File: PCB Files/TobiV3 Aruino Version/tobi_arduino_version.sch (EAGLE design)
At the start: 56 parts, among them M1 M1_M2, M2 M1_M2, M3 DF11-4PIN, M4 DF11-4PIN, M5 DF11-4PIN, M6 DF11-4PIN

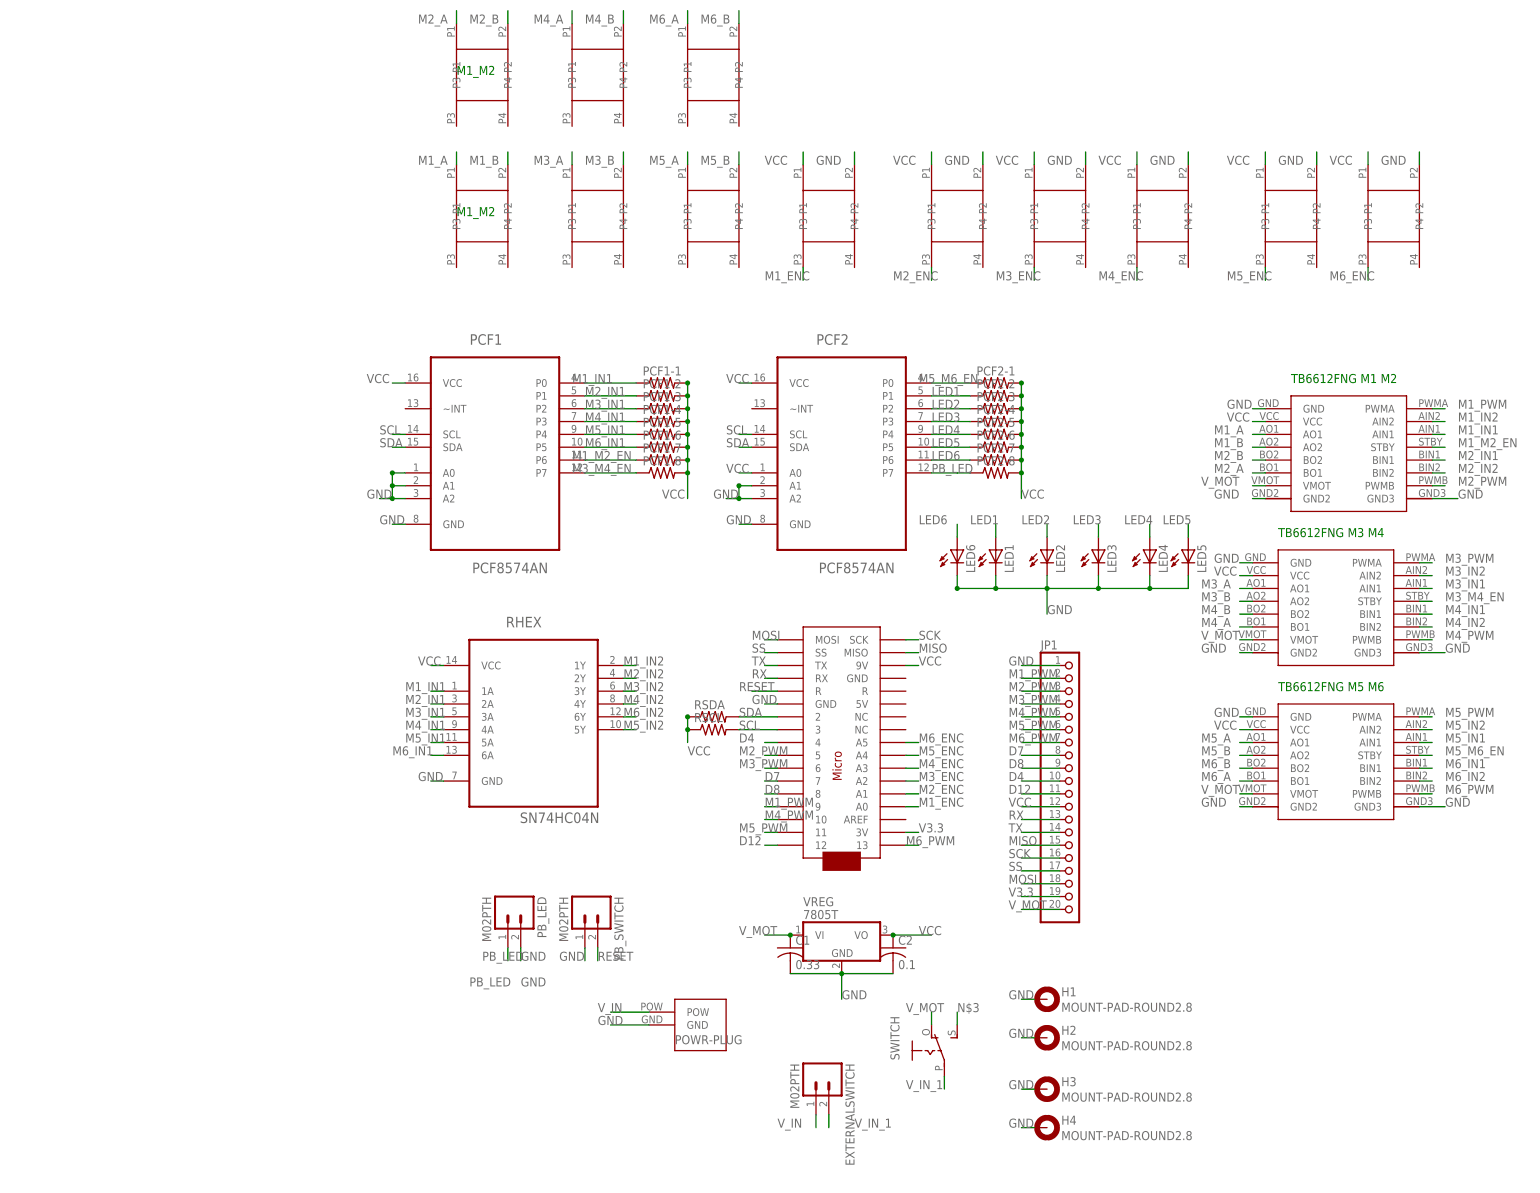
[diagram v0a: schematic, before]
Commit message: removed hex encoder, moved to 0-based
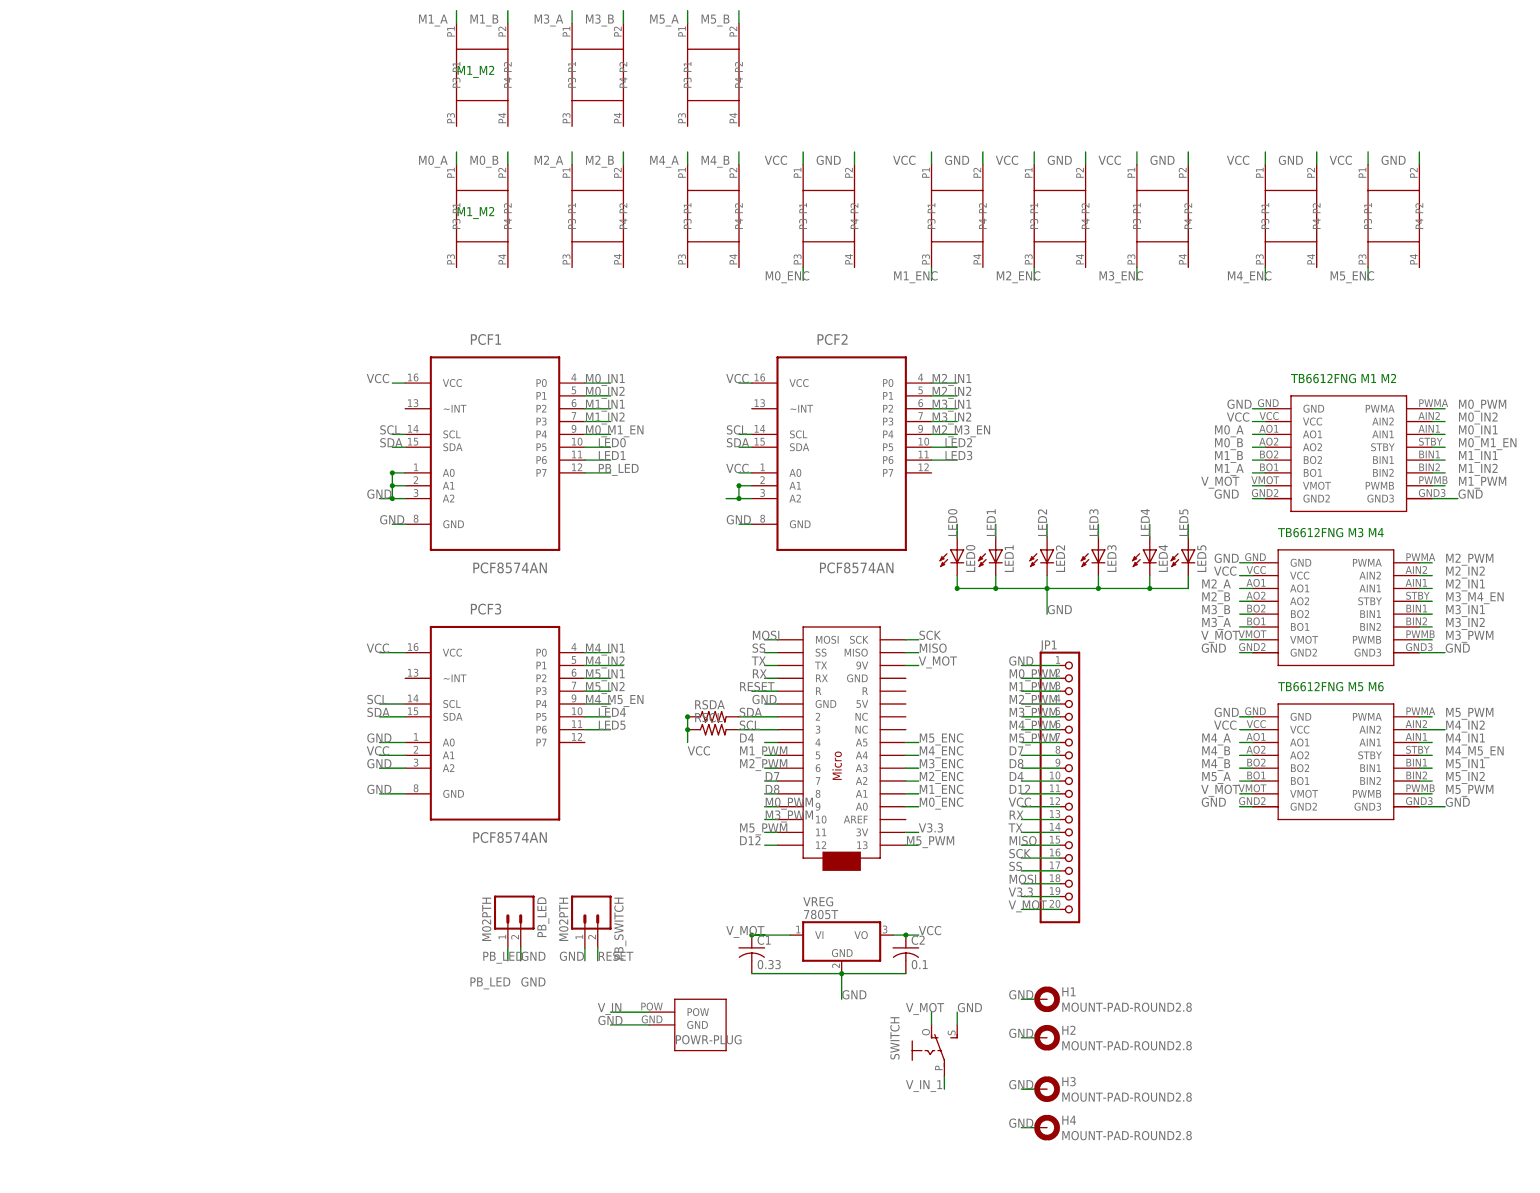
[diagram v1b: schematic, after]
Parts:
- removed EXTERNALSWITCH: M02PTH, SparkFun-Connectors:M02PTH
- removed PCF1-1, PCF1-2, PCF1-3, PCF1-4, PCF1-5, PCF1-6, PCF1-7, PCF1-8, PCF2-1, PCF2-2, PCF2-3, PCF2-4, PCF2-5, PCF2-6, PCF2-7, PCF2-8: (no value), rcl:R-US_0207/7
- removed RHEX: SN74HC04N, Texas Instruments_By_element14_Batch_1:SN74HC04N
- added PCF3: PCF8574AN, Texas Instruments_By_element14_Batch_1:PCF8574AN
- renumbered LED6 to LED0
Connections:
- removed net LED6: LED0.A, PCF2-7.1, PCF2.P6
- removed net M1_M2_EN: DRIVER1.STBY, PCF1-7.1, PCF1.P6
- removed net M5_M6_EN: DRIVER3.STBY, PCF2-1.1, PCF2.P0
- removed net M6_A: DRIVER3.BO1, M6.P1
- removed net M6_B: DRIVER3.BO2, M6.P2
- removed net M6_ENC: ARDUINOMICRO.A5, ENC6.P3
- removed net M6_IN1: DRIVER3.BIN1, PCF1-6.1, PCF1.P5, RHEX.6A
- removed net M6_IN2: DRIVER3.BIN2, RHEX.6Y
- removed net M6_PWM: ARDUINOMICRO.13, DRIVER3.PWMB, JP1.7
- removed net N$3: SWITCH.S
- new net LED0: LED0.A, PCF1.P5
- new net M0_A: DRIVER1.AO1, M1.P1
- new net M0_B: DRIVER1.AO2, M1.P2
- new net M0_ENC: ARDUINOMICRO.A0, ENC1.P3
- new net M0_IN1: DRIVER1.AIN1, PCF1.P0
- new net M0_IN2: DRIVER1.AIN2, PCF1.P1
- new net M0_M1_EN: DRIVER1.STBY, PCF1.P4
- new net M0_PWM: ARDUINOMICRO.9, DRIVER1.PWMA, JP1.2
- new net M2_M3_EN: PCF2.P4
- new net M4_M5_EN: DRIVER3.STBY, PCF3.P4
- net GND: now also PCF3.A0, PCF3.A2, PCF3.GND, SWITCH.S; no longer RHEX.GND
- net LED1: now also PCF1.P6; no longer PCF2-2.1, PCF2.P1
- net LED2: now also PCF2.P5; no longer PCF2-3.1, PCF2.P2
- net LED3: now also PCF2.P6; no longer PCF2-4.1, PCF2.P3
- net LED4: now also PCF3.P5; no longer PCF2-5.1, PCF2.P4
- net LED5: now also PCF3.P6; no longer PCF2-6.1, PCF2.P5
- net M1_A: now also DRIVER1.BO1, M2.P1; no longer DRIVER1.AO1, M1.P1
- net M1_B: now also DRIVER1.BO2, M2.P2; no longer DRIVER1.AO2, M1.P2
- net M1_ENC: now also ARDUINOMICRO.A1, ENC2.P3; no longer ARDUINOMICRO.A0, ENC1.P3
- net M1_IN1: now also DRIVER1.BIN1, PCF1.P2; no longer DRIVER1.AIN1, PCF1-1.1, PCF1.P0, RHEX.1A
- net M1_IN2: now also DRIVER1.BIN2, PCF1.P3; no longer DRIVER1.AIN2, RHEX.1Y
- net M1_PWM: now also ARDUINOMICRO.5, DRIVER1.PWMB, JP1.3; no longer ARDUINOMICRO.9, DRIVER1.PWMA, JP1.2
- net M2_A: now also DRIVER2.AO1, M3.P1; no longer DRIVER1.BO1, M2.P1
- net M2_B: now also DRIVER2.AO2, M3.P2; no longer DRIVER1.BO2, M2.P2
- net M2_ENC: now also ARDUINOMICRO.A2, ENC3.P3; no longer ARDUINOMICRO.A1, ENC2.P3
- net M2_IN1: now also DRIVER2.AIN1, PCF2.P0; no longer DRIVER1.BIN1, PCF1-2.1, PCF1.P1, RHEX.2A
- net M2_IN2: now also DRIVER2.AIN2, PCF2.P1; no longer DRIVER1.BIN2, RHEX.2Y
- net M2_PWM: now also ARDUINOMICRO.6, DRIVER2.PWMA, JP1.4; no longer ARDUINOMICRO.5, DRIVER1.PWMB, JP1.3
- net M3_A: now also DRIVER2.BO1, M4.P1; no longer DRIVER2.AO1, M3.P1
- net M3_B: now also DRIVER2.BO2, M4.P2; no longer DRIVER2.AO2, M3.P2
- net M3_ENC: now also ARDUINOMICRO.A3, ENC4.P3; no longer ARDUINOMICRO.A2, ENC3.P3
- net M3_IN1: now also DRIVER2.BIN1, PCF2.P2; no longer DRIVER2.AIN1, PCF1-3.1, PCF1.P2, RHEX.3A
- net M3_IN2: now also DRIVER2.BIN2, PCF2.P3; no longer DRIVER2.AIN2, RHEX.3Y
- net M3_M4_EN: no longer PCF1-8.1, PCF1.P7
- net M3_PWM: now also ARDUINOMICRO.10, DRIVER2.PWMB, JP1.5; no longer ARDUINOMICRO.6, DRIVER2.PWMA, JP1.4
- net M4_A: now also DRIVER3.AO1, M5.P1; no longer DRIVER2.BO1, M4.P1
- net M4_B: now also DRIVER3.AO2, DRIVER3.BO2, M5.P2; no longer DRIVER2.BO2, M4.P2
- net M4_ENC: now also ARDUINOMICRO.A4, ENC5.P3; no longer ARDUINOMICRO.A3, ENC4.P3
- net M4_IN1: now also DRIVER3.AIN1, PCF3.P0; no longer DRIVER2.BIN1, PCF1-4.1, PCF1.P3, RHEX.4A
- net M4_IN2: now also DRIVER3.AIN2, PCF3.P1; no longer DRIVER2.BIN2, RHEX.4Y
- net M4_PWM: now also JP1.6; no longer ARDUINOMICRO.10, DRIVER2.PWMB, JP1.5
- net M5_A: now also DRIVER3.BO1, M6.P1; no longer DRIVER3.AO1, M5.P1
- net M5_B: now also M6.P2; no longer DRIVER3.AO2, M5.P2
- net M5_ENC: now also ARDUINOMICRO.A5, ENC6.P3; no longer ARDUINOMICRO.A4, ENC5.P3
- net M5_IN1: now also DRIVER3.BIN1, PCF3.P2; no longer DRIVER3.AIN1, PCF1-5.1, PCF1.P4, RHEX.5A
- net M5_IN2: now also DRIVER3.BIN2, PCF3.P3; no longer DRIVER3.AIN2, RHEX.5Y
- net M5_PWM: now also ARDUINOMICRO.13, DRIVER3.PWMB, JP1.7; no longer JP1.6
- net PB_LED: now also PCF1.P7; no longer PCF2-8.1, PCF2.P7
- net SCL: now also PCF3.SCL
- net SDA: now also PCF3.SDA
- net VCC: now also PCF3.A1, PCF3.VCC; no longer ARDUINOMICRO.9V, PCF1-1.2, PCF1-2.2, PCF1-3.2, PCF1-4.2, PCF1-5.2, PCF1-6.2, PCF1-7.2, PCF1-8.2, PCF2-1.2, PCF2-2.2, PCF2-3.2, PCF2-4.2, PCF2-5.2, PCF2-6.2, PCF2-7.2, PCF2-8.2, RHEX.VCC
- net V_IN: no longer EXTERNALSWITCH.1
- net V_IN_1: no longer EXTERNALSWITCH.2
- net V_MOT: now also ARDUINOMICRO.9V
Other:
- moved on the sheet: C1, C2

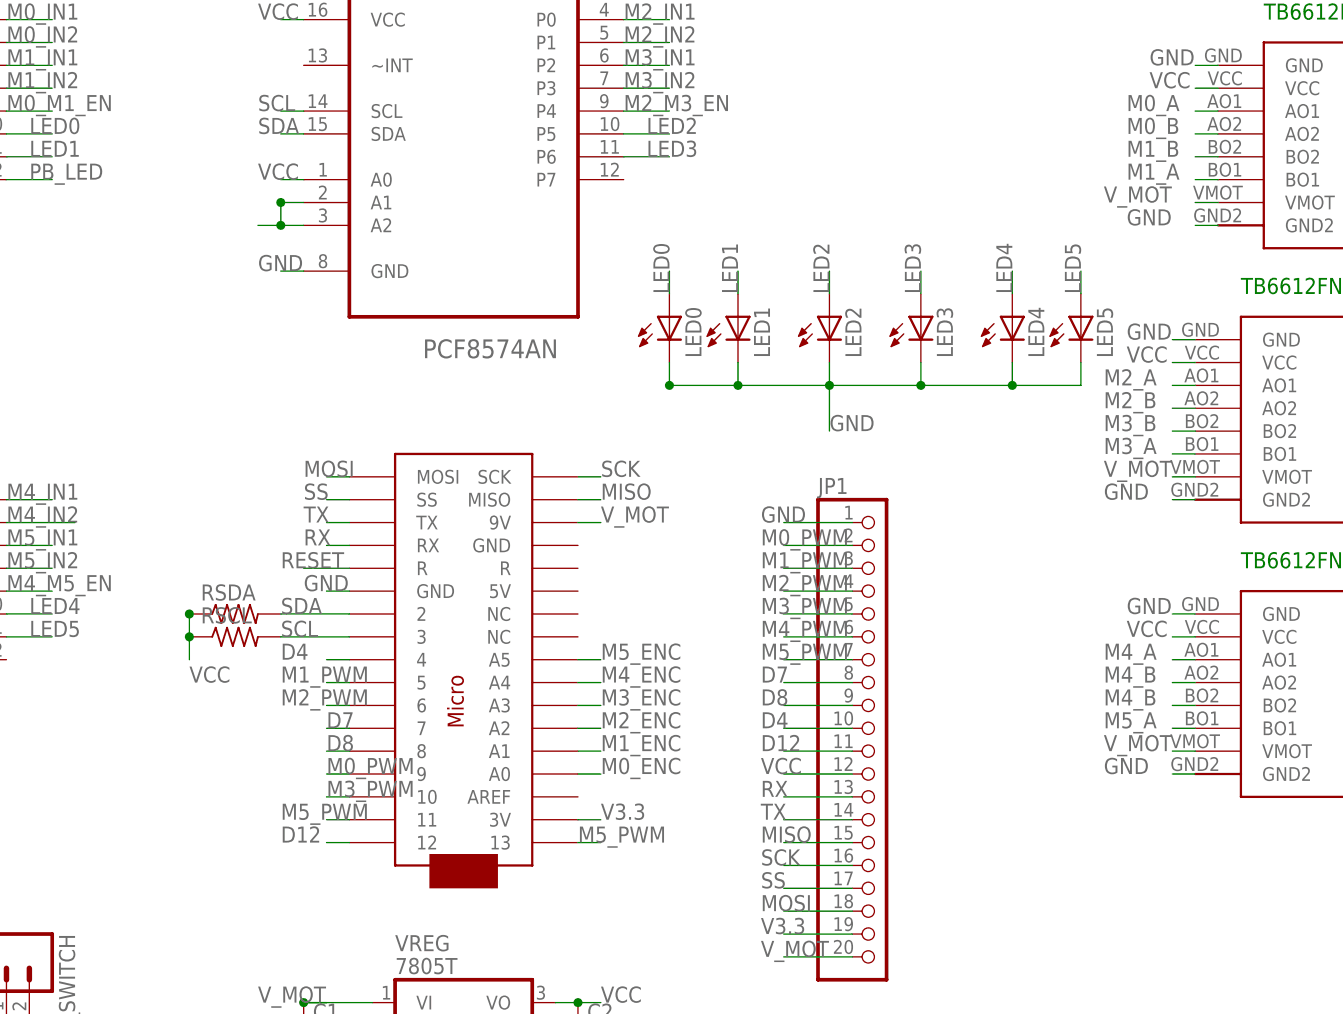
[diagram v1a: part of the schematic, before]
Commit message: changed pwm pins, added series LED resistors
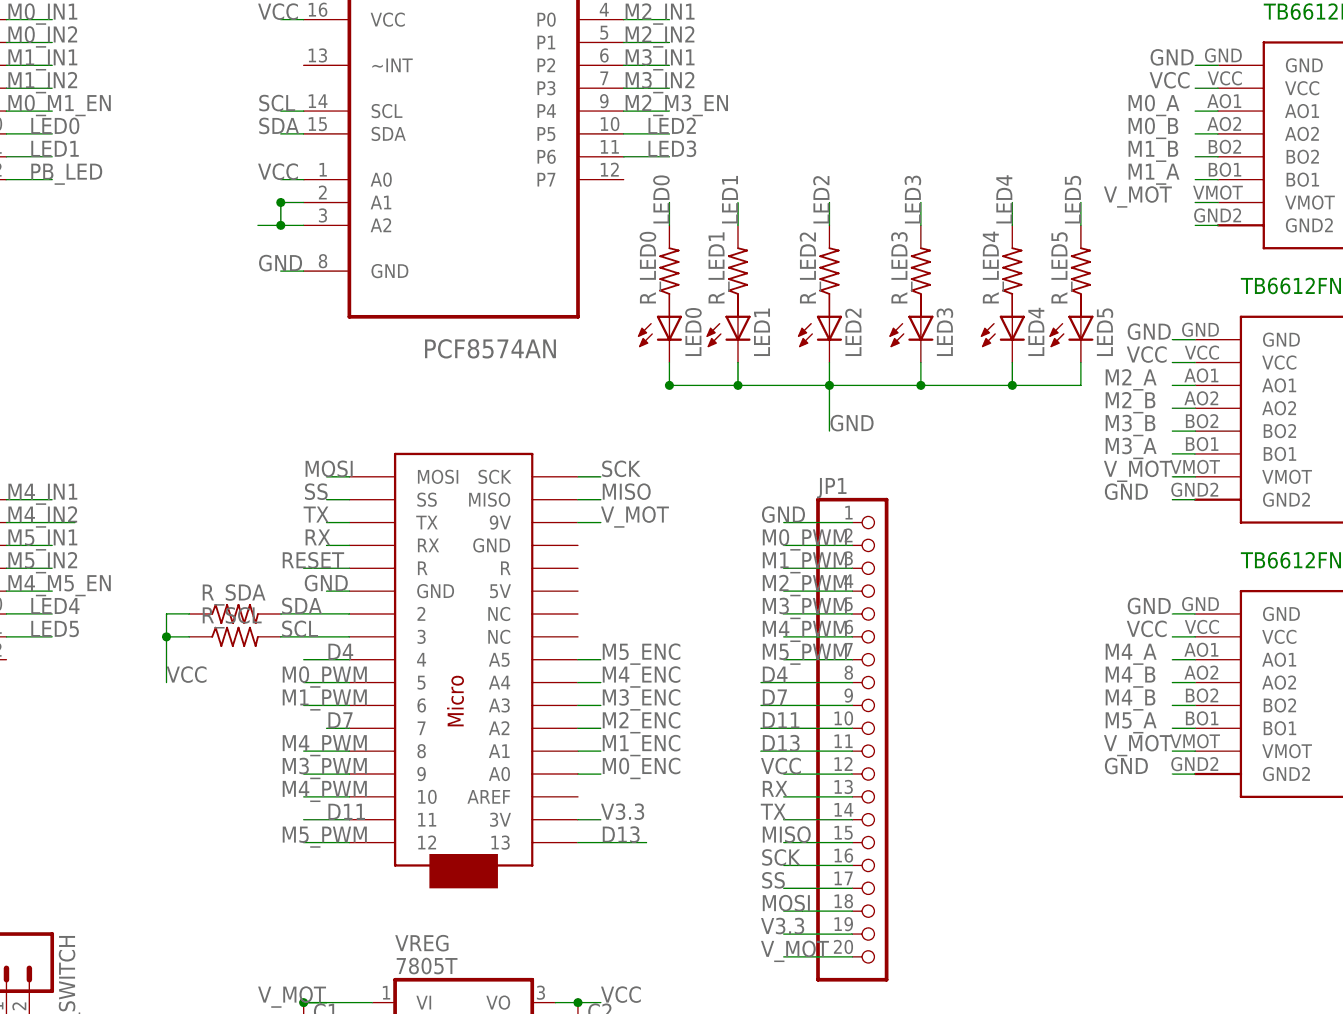
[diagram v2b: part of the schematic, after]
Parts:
- removed RSCL, RSDA: (no value), rcl:R-US_0207/7
- added R_LED0, R_LED1, R_LED2, R_LED3, R_LED4, R_LED5, R_SCL, R_SDA: (no value), resistor:R-US_0204/2V
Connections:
- removed net D12: ARDUINOMICRO.12, JP1.11
- removed net D8: ARDUINOMICRO.8, JP1.9
- new net D11: ARDUINOMICRO.11, JP1.10
- new net D13: ARDUINOMICRO.13, JP1.11
- net D4: now also JP1.8; no longer JP1.10
- net D7: now also JP1.9; no longer JP1.8
- net LED0: now also R_LED0.2; no longer LED0.A
- net LED1: now also R_LED1.2; no longer LED1.A
- net LED2: now also R_LED2.2; no longer LED2.A
- net LED3: now also R_LED3.2; no longer LED3.A
- net LED4: now also R_LED4.2; no longer LED4.A
- net LED5: now also R_LED5.2; no longer LED5.A
- net M0_PWM: now also ARDUINOMICRO.5; no longer ARDUINOMICRO.9
- net M1_PWM: now also ARDUINOMICRO.6; no longer ARDUINOMICRO.5
- net M2_PWM: no longer ARDUINOMICRO.6
- net M3_PWM: now also ARDUINOMICRO.9; no longer ARDUINOMICRO.10
- net M4_PWM: now also ARDUINOMICRO.10, ARDUINOMICRO.8
- net M5_PWM: now also ARDUINOMICRO.12; no longer ARDUINOMICRO.11, ARDUINOMICRO.13
- net SCL: now also R_SCL.2; no longer RSCL.2
- net SDA: now also R_SDA.2; no longer RSDA.2
- net VCC: now also R_SCL.1, R_SDA.1; no longer RSCL.1, RSDA.1

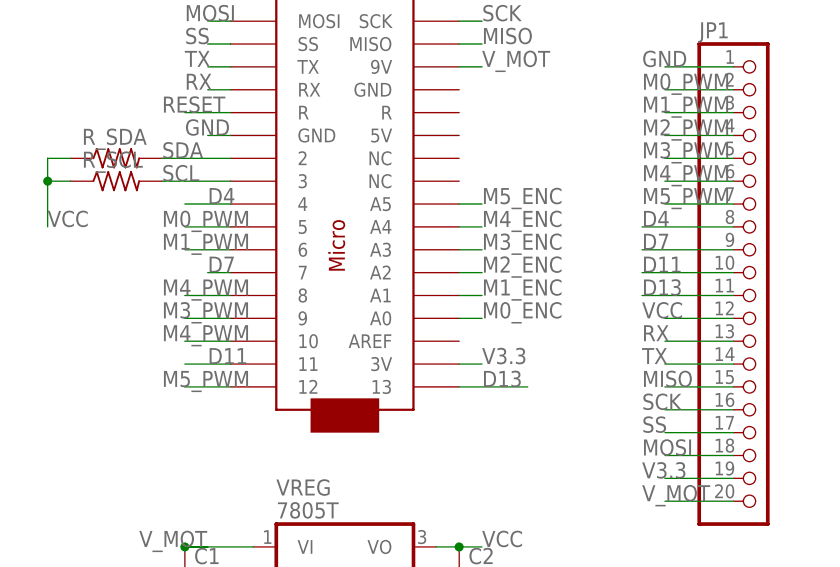
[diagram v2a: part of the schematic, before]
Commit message: fix motor pwm pins
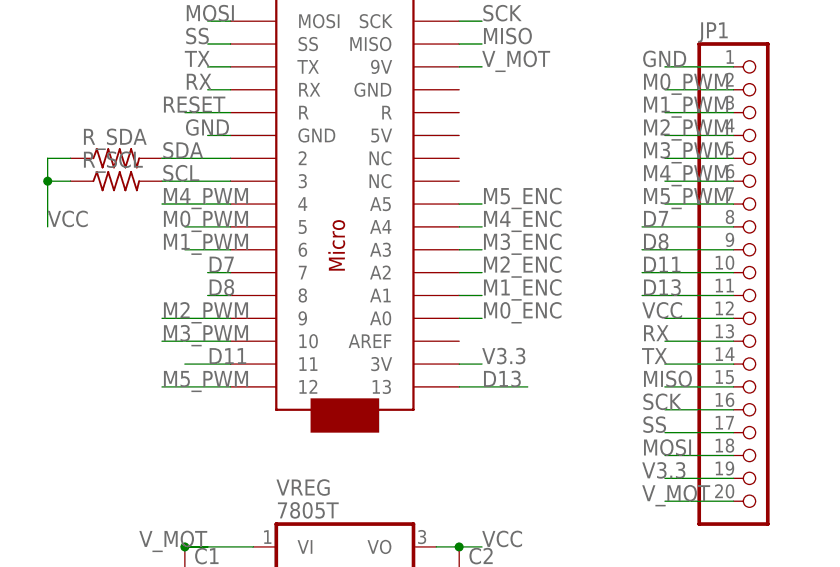
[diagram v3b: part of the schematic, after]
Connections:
- removed net D4: ARDUINOMICRO.4, JP1.8
- new net D8: ARDUINOMICRO.8, JP1.9
- net D7: now also JP1.8; no longer JP1.9
- net M2_PWM: now also ARDUINOMICRO.9
- net M3_PWM: now also ARDUINOMICRO.10; no longer ARDUINOMICRO.9
- net M4_PWM: now also ARDUINOMICRO.4; no longer ARDUINOMICRO.10, ARDUINOMICRO.8
